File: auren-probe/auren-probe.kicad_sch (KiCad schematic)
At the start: 11 parts, among them J1 HDMI_Micro-D_Molex_46765-1x01, J3 Speaker_1, J4 Speaker_2

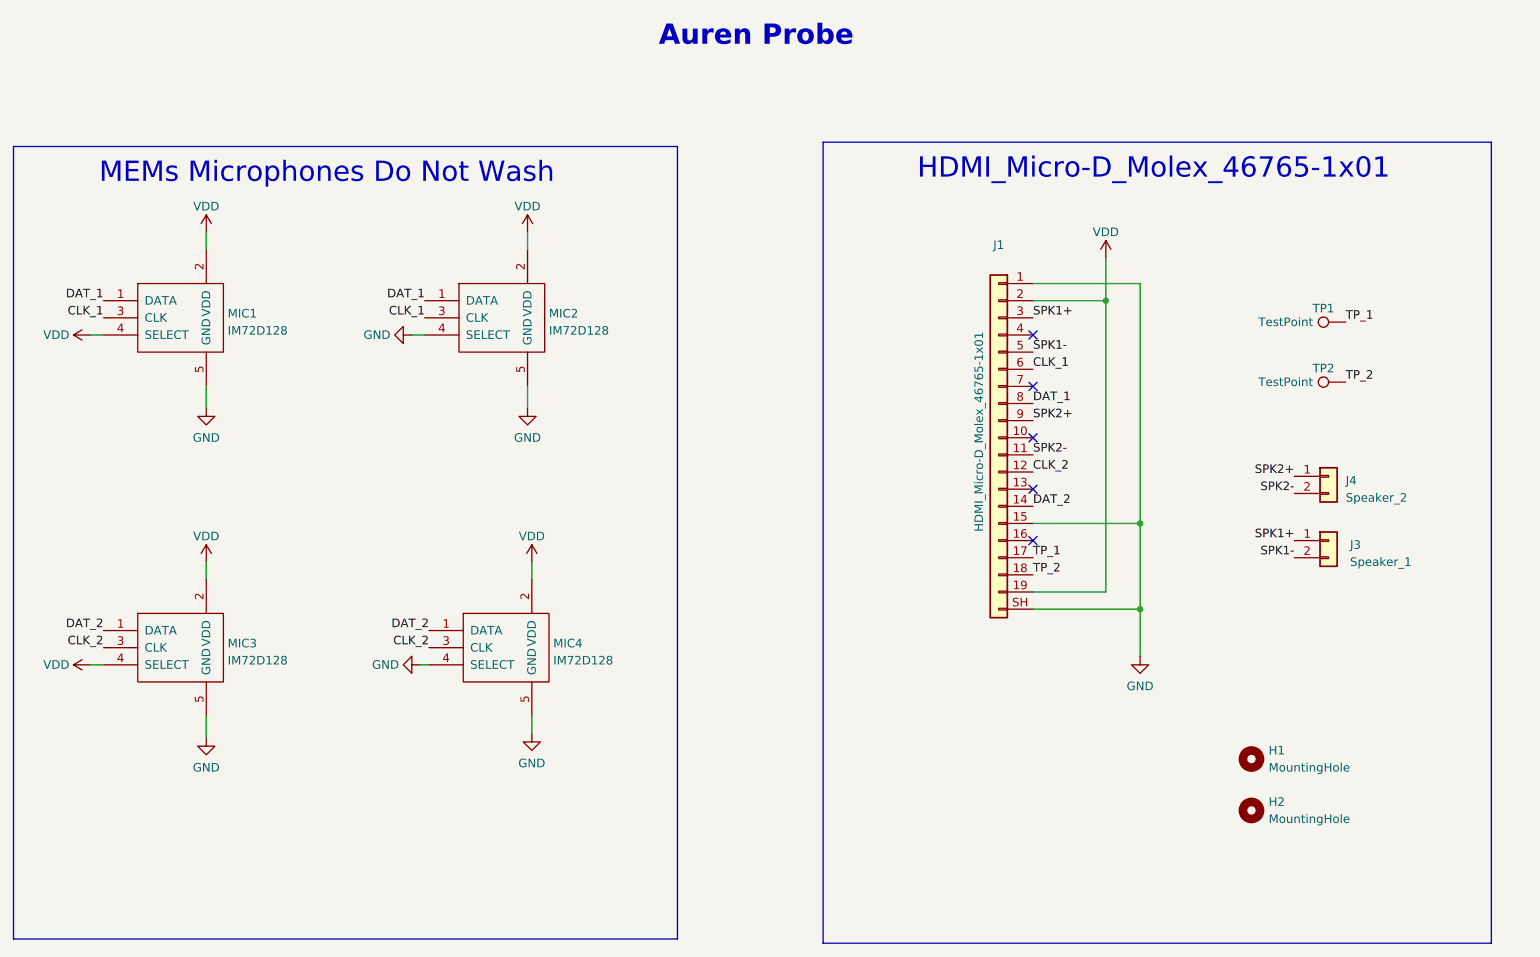
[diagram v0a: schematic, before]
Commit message: Major update
Added Rs on the DAT lines and Cs for each MIC.
Fixed footprint bugs and passing DRC
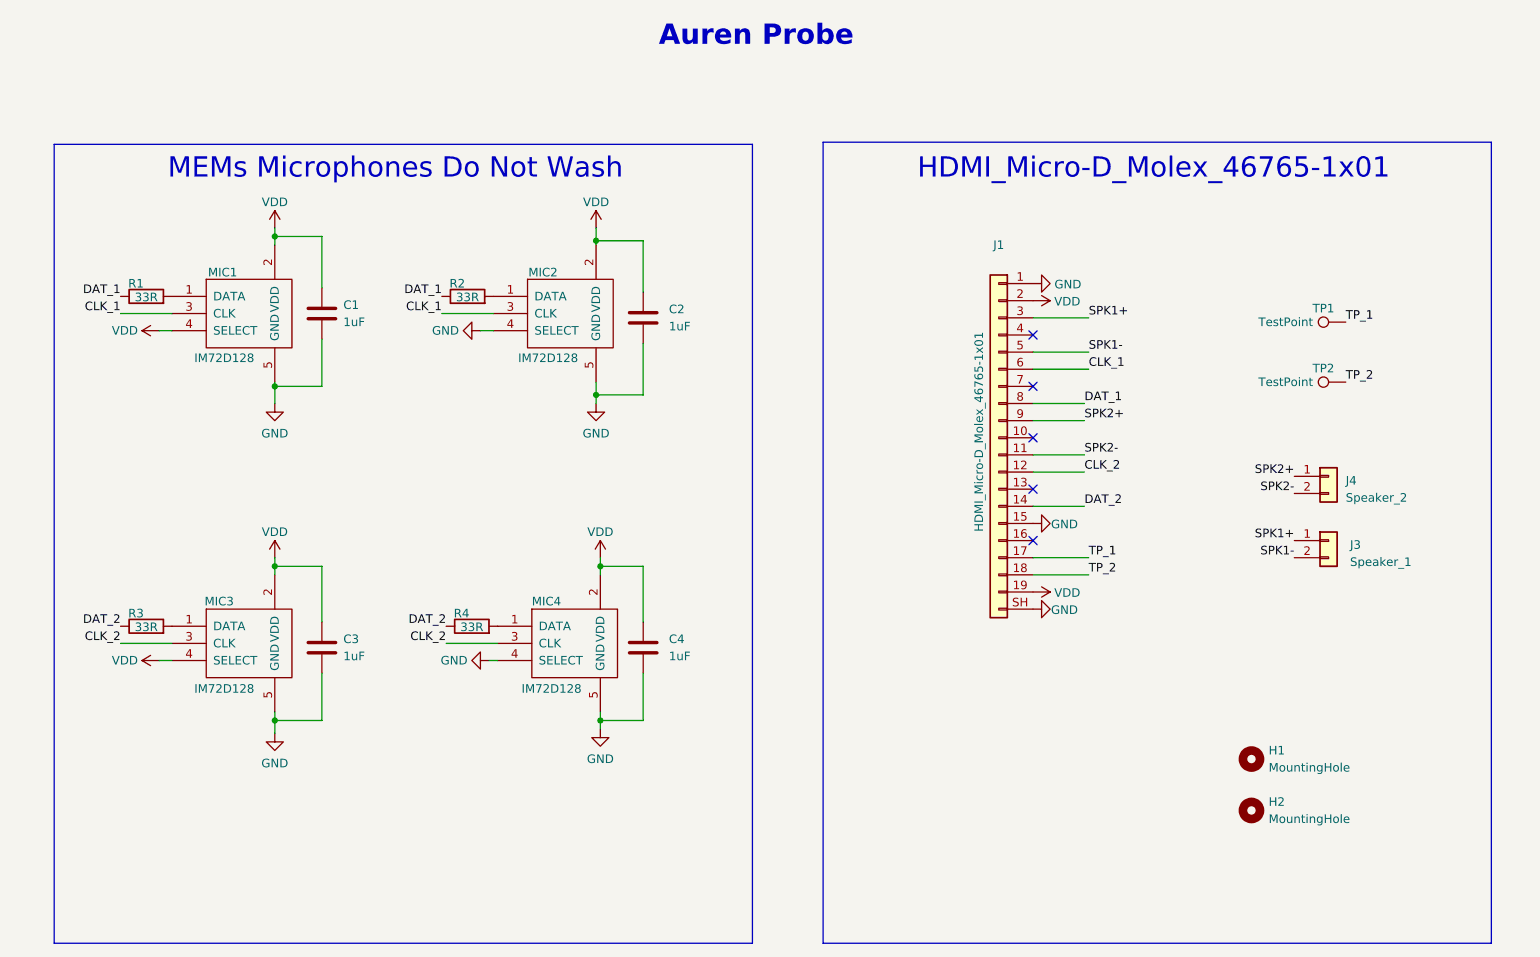
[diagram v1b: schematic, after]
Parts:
- added C1, C2, C3, C4: 1uF, Capacitor_SMD:C_0402_1005Metric, symbol Device:C
- added R1, R2, R3, R4: 33R, Resistor_SMD:R_0402_1005Metric, symbol Device:R
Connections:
- net DAT_1: now also R1.1, R2.1; no longer MIC1.1 (DATA), MIC2.1 (DATA)
- net DAT_2: now also R3.1, R4.1; no longer MIC3.1 (DATA), MIC4.1 (DATA)
- net GND: now also C1.2, C2.2, C3.2, C4.2
- net VDD: now also C1.1, C2.1, C3.1, C4.1
- new net: MIC4.1 (DATA), R4.2
- new net: MIC2.1 (DATA), R2.2
- new net: MIC3.1 (DATA), R3.2
- new net: MIC1.1 (DATA), R1.2
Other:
- moved on the sheet: MIC1, MIC2, MIC3, MIC4
